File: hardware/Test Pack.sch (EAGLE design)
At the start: 88 parts, among them Q1 BSS138, U1 BQ7694040

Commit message: Firmware, test pack layouts.
Firmware is mostly working! Layouts are pretty good.
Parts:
- removed C1: 4.7uF, SparkFun-Capacitors:4.7UF-6.3V-10%(0603)0603
- removed C10, C2, C9: 4700pF, SparkFun-Capacitors:4.7NF-50V-10%(0603)
- removed C11, C12, C13, C14, C15, C16, C17, C18, C19, C20, C21, C22, C23, C24, C25, C26, C27, C28, C4, C6, C7, C8: 1uF, SparkFun-Capacitors:1.0UF-16V-10%(0603)
- removed C29, C30, C31: 0.1uF, SparkFun-Capacitors:0.1UF-25V(+80/-20%)(0603)
- removed C32, C33, C34: 10uF, SparkFun-Capacitors:10UF50V20%(1210)
- removed D1, D2, D3: BAS16, SparkFun-DiscreteSemi:DIODESOD
- removed JP10: (no value), SparkFun-Connectors:M05PTH
- removed JP6, JP8, JP9: M02PTH, SparkFun-Connectors:M02PTH
- removed Q1: BSS138, SparkFun-DiscreteSemi:MOSFET-NCHANNELBSS138
- removed R1, R2, R32, R33, R34: 10k, SparkFun-Resistors:10KOHM1/10W1%(0603)0603
- removed R10, R11, R12, R13, R14, R15, R16, R17, R18, R19, R20, R21, R22, R23, R24, R4, R5, R6: 1K, SparkFun-Resistors:1KOHM1/10W1%(0603)
- removed R25, R26: 4.7k, SparkFun-Resistors:4.7KOHM1/10W1%(0603)
- removed R27, R28, R3, R30, R31: 100, SparkFun-Resistors:100OHM1/10W1%(0603)
- removed R29: .001, bq769x0:RESISTORWSR
- removed S1: BOOT, SparkFun-Electromechanical:SWITCH-MOMENTARY-2-SMD-1101NE
- removed SJ1: (no value), SparkFun-Passives:JUMPER-PAD-3-NC_BY_TRACE
- removed SJ2, SJ3, SJ4: JUMPER-PAD-2-NC_BY_TRACE, SparkFun-Passives:JUMPER-PAD-2-NC_BY_TRACE
- removed U1: BQ7694040, bq769x0:BQ7694040
- added B1, B10, B11, B12, B13, B14, B15, B2, B3, B4, B5, B6, B7, B8, B9: BATTERY18650, bq769x0:BATTERY18650
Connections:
- removed net ALERT: JP10.1, R25.2, U1.ALERT
- removed net BATT: C32.1, D1.C, R3.2, U1.BAT
- removed net CAP2: C4.1, U1.CAP2, U1.NC@11, U1.NC@12
- removed net CAP3: C6.1, U1.CAP3, U1.NC@16, U1.NC@17
- removed net CHG: U1.CHG
- removed net DSG: U1.DSG
- removed net GND: C1.2, C11.1, C12.2, C2.2, C34.2, C7.2, C8.2, JP10.5, JP4.1, JP6.1, JP8.1, JP9.1, R25.1, R27.1, R29.1, R32.1, R33.1, R34.1, R4.1, U1.VSS
- removed net N$10: R2.2, SJ1.3
- removed net N$11: R1.2, SJ1.1
- removed net N$28: R33.2, SJ3.1
- removed net N$3: R32.2, SJ2.1
- removed net N$30: C7.1, U1.CAP1
- removed net N$32: R26.1, S1.2
- removed net N$33: R34.2, SJ4.1
- removed net N$34: C29.2, C30.2, R27.2
- removed net N$35: C30.1, C31.1, R28.2
- removed net REGOUT: C1.1, JP10.2, SJ1.2, U1.REGOUT
- removed net REGSRC: C8.1, Q1.S, U1.REGSRC
- removed net SCL: JP10.4, R1.1, U1.SCL
- removed net SDA: JP10.3, R2.1, U1.SDA
- removed net SRN: C31.2, U1.SRN
- removed net SRP: C29.1, U1.SRP
- removed net TS1: C2.1, JP8.2, R26.2, SJ2.2, U1.TS1
- removed net TS2: C9.1, JP6.2, SJ3.2, U1.TS2
- removed net TS3: C10.1, JP9.2, SJ4.2, U1.TS3
- removed net VC0: C11.2, R4.2, U1.VC0
- removed net VC1: C12.1, C13.2, R5.2, U1.VC1
- removed net VC10: C21.1, D2.A, R17.2, U1.VC10
- removed net VC10B: C22.2, R20.2, U1.VC10B
- removed net VC10X: C10.2, C22.1, C25.2, C32.2, C33.1, C6.2, D2.C, R30.1, U1.VC10X
- removed net VC11: C23.2, C25.1, R18.2, U1.VC11
- removed net VC12: C23.1, C26.2, R21.2, U1.VC12
- removed net VC13: C26.1, C27.2, R22.2, U1.VC13
- removed net VC14: C27.1, C28.2, R23.2, U1.VC14
- removed net VC15: C28.1, D1.A, R24.2, U1.VC15
- removed net VC2: C13.1, C14.2, R6.2, U1.VC2
- removed net VC3: C14.1, C15.2, R10.2, U1.VC3
- removed net VC4: C15.1, C16.2, R11.2, U1.VC4
- removed net VC5: C16.1, D3.A, R12.2, U1.VC5
- removed net VC5B: C24.2, R13.2, U1.VC5B
- removed net VC5X: C17.2, C24.1, C33.2, C34.1, C4.2, C9.2, D3.C, Q1.G, R31.1, U1.VC5X
- removed net VC6: C17.1, C18.2, R19.2, U1.VC6
- removed net VC7: C18.1, C19.2, R14.2, U1.VC7
- removed net VC8: C19.1, C20.2, R15.2, U1.VC8
- removed net VC9: C20.1, C21.2, R16.2, U1.VC9
- net CELL1: now also B1.+, B2.-; no longer R5.1, S1.1
- net CELL10: now also B10.+, B11.-; no longer R17.1, R20.1, R30.2
- net CELL11: now also B11.+, B12.-; no longer R18.1
- net CELL12: now also B12.+, B13.-; no longer R21.1
- net CELL13: now also B13.+, B14.-; no longer R22.1
- net CELL14: now also B14.+, B15.-; no longer R23.1
- net CELL2: now also B2.+, B3.-; no longer R6.1
- net CELL3: now also B3.+, B4.-; no longer R10.1
- net CELL4: now also B4.+, B5.-; no longer R11.1
- net CELL5: now also B5.+, B6.-; no longer R12.1, R13.1, R31.2
- net CELL6: now also B6.+, B7.-; no longer R19.1
- net CELL7: now also B7.+, B8.-; no longer R14.1
- net CELL8: now also B8.+, B9.-; no longer R15.1
- net CELL9: now also B10.-, B9.+; no longer R16.1
- net PACK+: now also B15.+; no longer Q1.D, R24.1, R3.1
- net PACK-: now also B1.-, JP4.1; no longer R28.1, R29.2
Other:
- note added: "Fix label alignment"
- note added: "The cells are labeled reverse"
- note removed: "3.3V I2C conversion"
- note removed: "A"
- note removed: "B"
- note removed: "Cut traces to enable thermistors"
- note removed: "Input on TS1 required to boot"
- note removed: "LOAD-"
- note removed: "May want 100 ohm into regsource"
- note removed: "May want 200 ohm resistor to pack +"
- note removed: "Over Current / Short Circuit Sense"
- note removed: "Swap resistor to 2512: CSR2512C0R001F"
- note removed: "Thermistors (optional)"
- note removed: "Thermistors have internally trimmed 10k pull up Do we need these pulldowns?"
- note removed: "This fet is not high enough V"
- note removed: "bq7694002, 15 cell, 0x08 I2C, 3.3V, no CRC"
- moved on the sheet: JP3, JP4, JP5, JP7

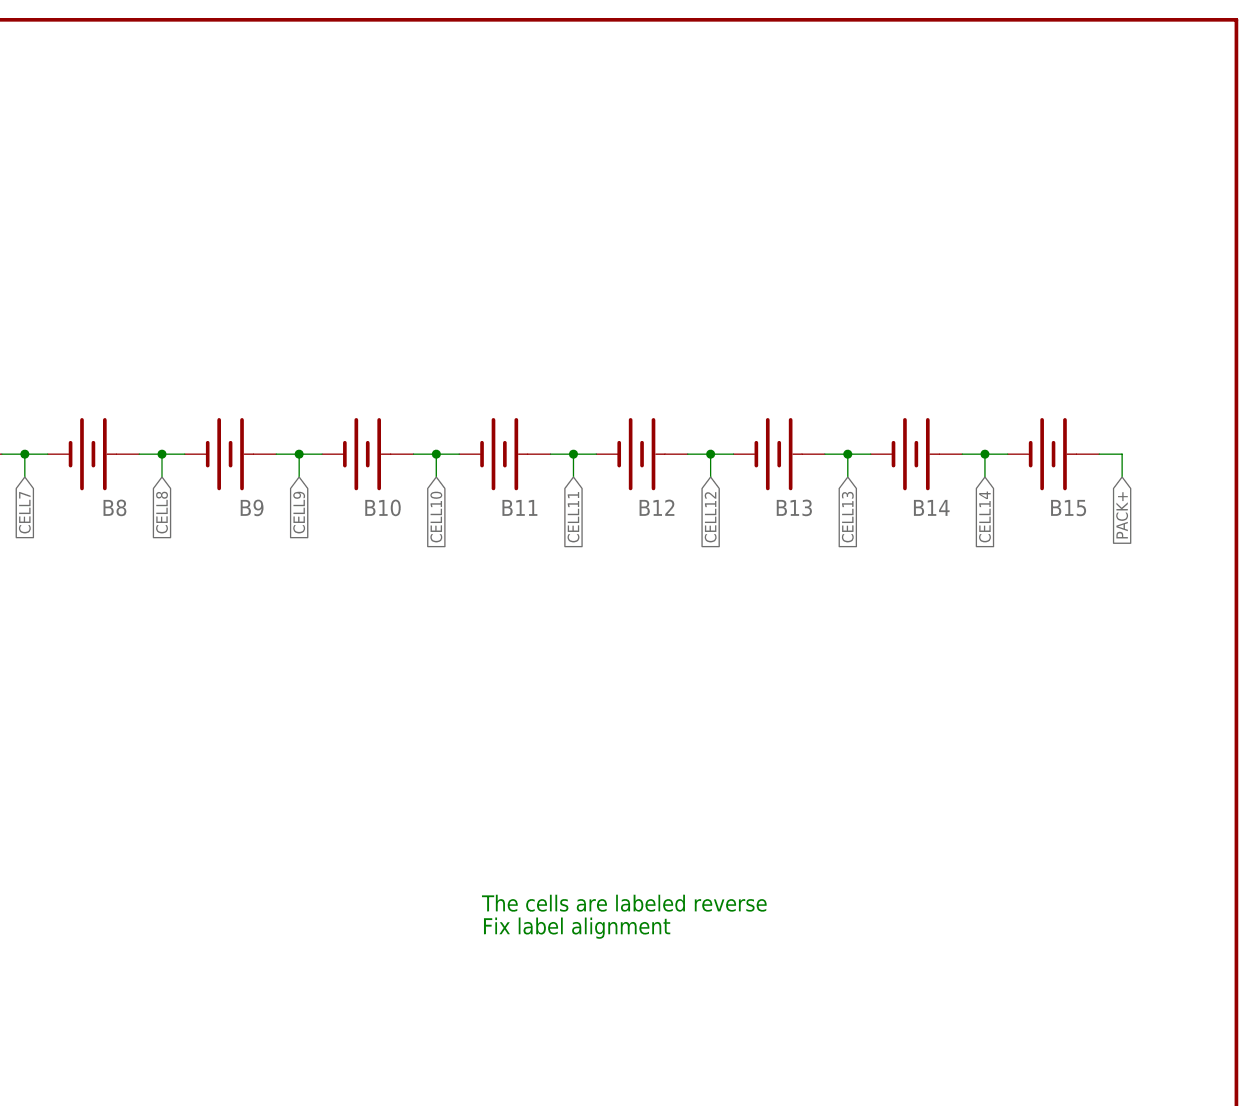
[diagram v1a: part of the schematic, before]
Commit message: v2 with Charge/Discharge MOSFET control and cell balancing
Many changes. Added large MOSFETs and pack interface circuitry. Added
small MOSFETs for individual cell balancing/charging. Corrected
Thermistor pull down error. All FPs pass 1:1 check.
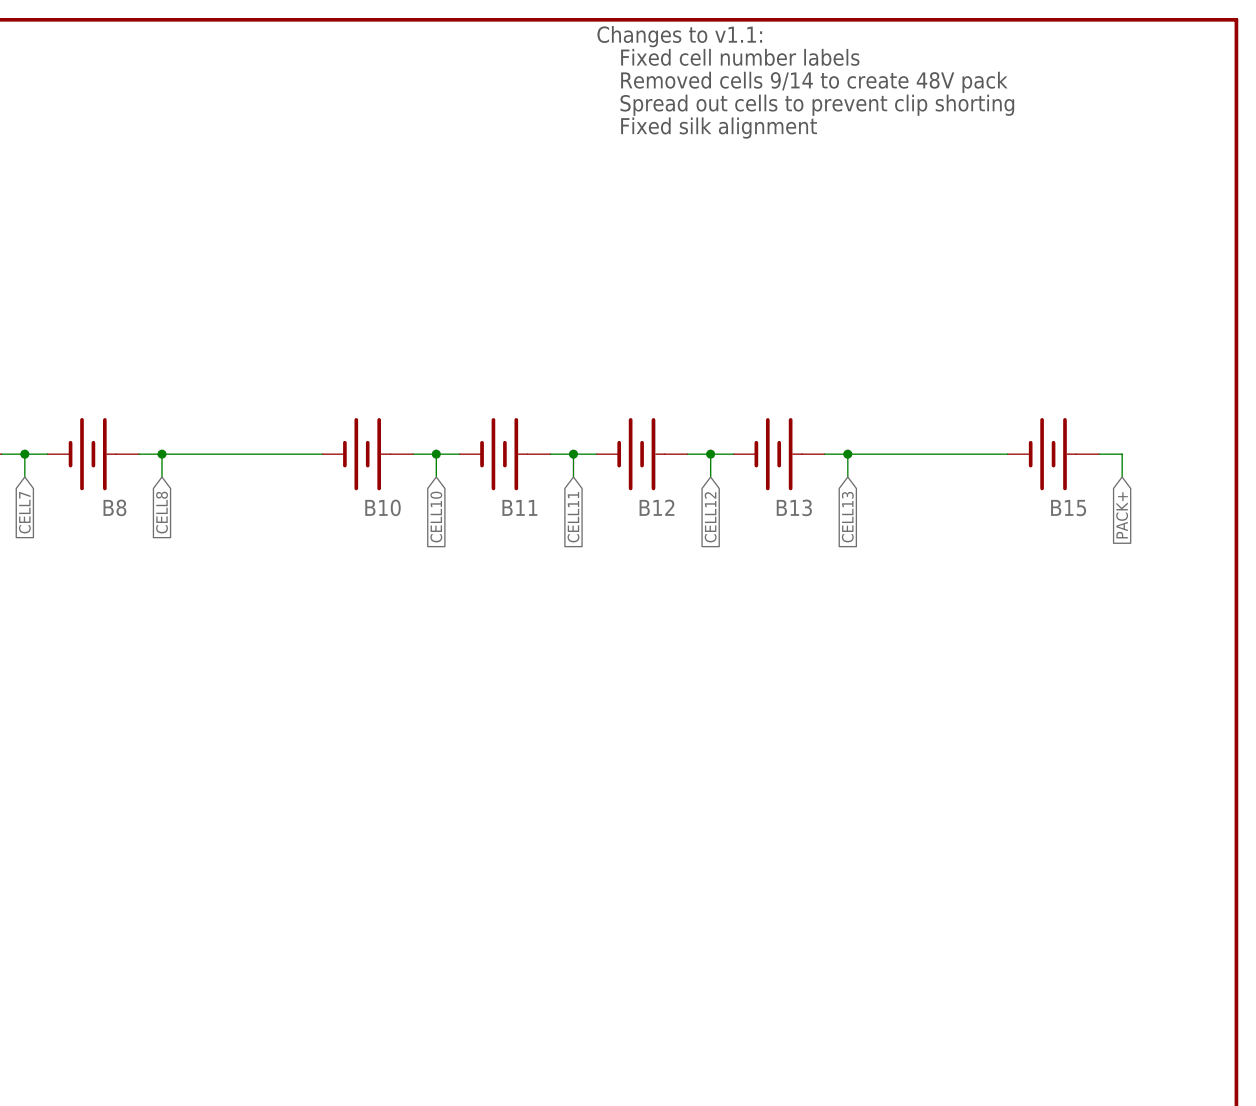
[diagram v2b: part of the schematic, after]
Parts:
- removed B14, B9: BATTERY18650, bq769x0:BATTERY18650
- B1, B10, B11, B12, B13, B15, B2, B3, B4, B5, B6, B7, B8: value BATTERY18650 -> (none); device bq769x0:BATTERY18650 -> SparkFun-Electromechanical:BATTERY18650
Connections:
- net CELL13: now also B15.-; no longer B14.-
- net CELL14: no longer B14.+, B15.-
- net CELL8: now also B10.-; no longer B9.-
- net CELL9: no longer B10.-, B9.+
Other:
- note added: "Changes to v1.1:"
- note added: "Fixed cell number labels"
- note added: "Fixed silk alignment"
- note added: "Removed cells 9/14 to create 48V pack"
- note added: "Spread out cells to prevent clip shorting"
- note removed: "Fix label alignment"
- note removed: "The cells are labeled reverse"
